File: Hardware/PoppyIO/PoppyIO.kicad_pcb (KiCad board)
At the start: 2 copper layers, 102 x 86 mm, 0 parts

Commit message: hw: io: Some PCB planning
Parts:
- added D10: Green, LED_SMD:LED_0805_2012Metric_Pad1.15x1.40mm_HandSolder, F.Cu at (132.4, 85.0)
- added D11: Green, LED_SMD:LED_0805_2012Metric_Pad1.15x1.40mm_HandSolder, F.Cu at (134.9, 85.0)
- added D12: Green, LED_SMD:LED_0805_2012Metric_Pad1.15x1.40mm_HandSolder, F.Cu at (137.5, 85.0)
- added D13: Green, LED_SMD:LED_0805_2012Metric_Pad1.15x1.40mm_HandSolder, F.Cu at (140.0, 85.0)
- added D14: Green, LED_SMD:LED_0805_2012Metric_Pad1.15x1.40mm_HandSolder, F.Cu at (145.4, 85.0)
- added D15: Green, LED_SMD:LED_0805_2012Metric_Pad1.15x1.40mm_HandSolder, F.Cu at (147.9, 85.0)
- added D16: Green, LED_SMD:LED_0805_2012Metric_Pad1.15x1.40mm_HandSolder, F.Cu at (150.5, 85.0)
- added D17: Green, LED_SMD:LED_0805_2012Metric_Pad1.15x1.40mm_HandSolder, F.Cu at (153.0, 85.0)
- added D18: Green, LED_SMD:LED_0805_2012Metric_Pad1.15x1.40mm_HandSolder, F.Cu at (106.4, 115.0)
- added D19: Green, LED_SMD:LED_0805_2012Metric_Pad1.15x1.40mm_HandSolder, F.Cu at (108.9, 115.0)
- added D2: Green, LED_SMD:LED_0805_2012Metric_Pad1.15x1.40mm_HandSolder, F.Cu at (106.4, 85.0)
- added D20: Green, LED_SMD:LED_0805_2012Metric_Pad1.15x1.40mm_HandSolder, F.Cu at (111.5, 115.0)
- added D21: Green, LED_SMD:LED_0805_2012Metric_Pad1.15x1.40mm_HandSolder, F.Cu at (114.0, 115.0)
- added D22: Green, LED_SMD:LED_0805_2012Metric_Pad1.15x1.40mm_HandSolder, F.Cu at (119.4, 115.0)
- added D23: Green, LED_SMD:LED_0805_2012Metric_Pad1.15x1.40mm_HandSolder, F.Cu at (121.9, 115.0)
- added D24: Green, LED_SMD:LED_0805_2012Metric_Pad1.15x1.40mm_HandSolder, F.Cu at (124.5, 115.0)
- added D25: Green, LED_SMD:LED_0805_2012Metric_Pad1.15x1.40mm_HandSolder, F.Cu at (127.0, 115.0)
- added D26: Green, LED_SMD:LED_0805_2012Metric_Pad1.15x1.40mm_HandSolder, F.Cu at (132.4, 115.0)
- added D27: Green, LED_SMD:LED_0805_2012Metric_Pad1.15x1.40mm_HandSolder, F.Cu at (134.9, 115.0)
- added D28: Green, LED_SMD:LED_0805_2012Metric_Pad1.15x1.40mm_HandSolder, F.Cu at (137.5, 115.0)
- added D29: Green, LED_SMD:LED_0805_2012Metric_Pad1.15x1.40mm_HandSolder, F.Cu at (140.0, 115.0)
- added D3: Green, LED_SMD:LED_0805_2012Metric_Pad1.15x1.40mm_HandSolder, F.Cu at (108.9, 85.0)
- added D30: Green, LED_SMD:LED_0805_2012Metric_Pad1.15x1.40mm_HandSolder, F.Cu at (145.4, 115.0)
- added D31: Green, LED_SMD:LED_0805_2012Metric_Pad1.15x1.40mm_HandSolder, F.Cu at (147.9, 115.0)
- added D32: Green, LED_SMD:LED_0805_2012Metric_Pad1.15x1.40mm_HandSolder, F.Cu at (150.5, 115.0)
- added D33: Green, LED_SMD:LED_0805_2012Metric_Pad1.15x1.40mm_HandSolder, F.Cu at (153.0, 115.0)
- added D4: Green, LED_SMD:LED_0805_2012Metric_Pad1.15x1.40mm_HandSolder, F.Cu at (111.5, 85.0)
- added D5: Green, LED_SMD:LED_0805_2012Metric_Pad1.15x1.40mm_HandSolder, F.Cu at (114.0, 85.0)
- added D6: Green, LED_SMD:LED_0805_2012Metric_Pad1.15x1.40mm_HandSolder, F.Cu at (119.4, 85.0)
- added D7: Green, LED_SMD:LED_0805_2012Metric_Pad1.15x1.40mm_HandSolder, F.Cu at (121.9, 85.0)
- added D8: Green, LED_SMD:LED_0805_2012Metric_Pad1.15x1.40mm_HandSolder, F.Cu at (124.5, 85.0)
- added D9: Green, LED_SMD:LED_0805_2012Metric_Pad1.15x1.40mm_HandSolder, F.Cu at (127.0, 85.0)
- added J1: TC2030-IDC, Connector:Tag-Connect_TC2030-IDC-FP_2x03_P1.27mm_Vertical, F.Cu at (169.0, 83.0)
- added J10: WAGO 233-508, PoppyLogicController:WAGO_233-204, F.Cu at (132.4, 135.0)
- added J11: WAGO 233-508, PoppyLogicController:WAGO_233-204, F.Cu at (145.4, 135.0)
- added J12: Conn_02x04_Counter_Clockwise, Connector_PinHeader_2.54mm:PinHeader_2x04_P2.54mm_Vertical, F.Cu at (194.7, 76.2)
- added J2: WAGO 233-508, PoppyLogicController:WAGO_233-204, F.Cu at (193.6, 65.0)
- added J3: WAGO 233-508, PoppyLogicController:WAGO_233-204, F.Cu at (114.0, 65.0)
- added J4: WAGO 233-508, PoppyLogicController:WAGO_233-204, F.Cu at (127.0, 65.0)
- added J5: WAGO 233-508, PoppyLogicController:WAGO_233-204, F.Cu at (140.0, 65.0)
- added J6: WAGO 233-508, PoppyLogicController:WAGO_233-204, F.Cu at (153.0, 65.0)
- added J7: WAGO 233-508, PoppyLogicController:WAGO_233-204, F.Cu at (186.0, 135.0)
- added J8: WAGO 233-508, PoppyLogicController:WAGO_233-204, F.Cu at (106.4, 135.0)
- added J9: WAGO 233-508, PoppyLogicController:WAGO_233-204, F.Cu at (119.4, 135.0)
- added R13: 1k, Resistor_SMD:R_0603_1608Metric_Pad0.98x0.95mm_HandSolder, F.Cu at (106.4, 80.0)
- added R14: 1k, Resistor_SMD:R_0603_1608Metric_Pad0.98x0.95mm_HandSolder, F.Cu at (108.9, 80.0)
- added R19: 1k, Resistor_SMD:R_0603_1608Metric_Pad0.98x0.95mm_HandSolder, F.Cu at (111.5, 80.0)
- added R20: 1k, Resistor_SMD:R_0603_1608Metric_Pad0.98x0.95mm_HandSolder, F.Cu at (114.0, 80.0)
- added R25: 1k, Resistor_SMD:R_0603_1608Metric_Pad0.98x0.95mm_HandSolder, F.Cu at (119.4, 80.0)
- added R26: 1k, Resistor_SMD:R_0603_1608Metric_Pad0.98x0.95mm_HandSolder, F.Cu at (121.9, 80.0)
- added R31: 1k, Resistor_SMD:R_0603_1608Metric_Pad0.98x0.95mm_HandSolder, F.Cu at (124.5, 80.0)
- added R32: 1k, Resistor_SMD:R_0603_1608Metric_Pad0.98x0.95mm_HandSolder, F.Cu at (127.0, 80.0)
- added R37: 1k, Resistor_SMD:R_0603_1608Metric_Pad0.98x0.95mm_HandSolder, F.Cu at (132.4, 80.0)
- added R38: 1k, Resistor_SMD:R_0603_1608Metric_Pad0.98x0.95mm_HandSolder, F.Cu at (134.9, 80.0)
- added R43: 1k, Resistor_SMD:R_0603_1608Metric_Pad0.98x0.95mm_HandSolder, F.Cu at (137.5, 80.0)
- added R44: 1k, Resistor_SMD:R_0603_1608Metric_Pad0.98x0.95mm_HandSolder, F.Cu at (140.0, 80.0)
- added R49: 1k, Resistor_SMD:R_0603_1608Metric_Pad0.98x0.95mm_HandSolder, F.Cu at (145.4, 80.0)
- added R50: 1k, Resistor_SMD:R_0603_1608Metric_Pad0.98x0.95mm_HandSolder, F.Cu at (147.9, 80.0)
- added R55: 1k, Resistor_SMD:R_0603_1608Metric_Pad0.98x0.95mm_HandSolder, F.Cu at (150.5, 80.0)
- added R56: 1k, Resistor_SMD:R_0603_1608Metric_Pad0.98x0.95mm_HandSolder, F.Cu at (153.0, 80.0)
- added R57: 1k, Resistor_SMD:R_0603_1608Metric_Pad0.98x0.95mm_HandSolder, F.Cu at (106.4, 120.0)
- added R58: 1k, Resistor_SMD:R_0603_1608Metric_Pad0.98x0.95mm_HandSolder, F.Cu at (108.9, 120.0)
- added R59: 1k, Resistor_SMD:R_0603_1608Metric_Pad0.98x0.95mm_HandSolder, F.Cu at (111.5, 120.0)
- added R60: 1k, Resistor_SMD:R_0603_1608Metric_Pad0.98x0.95mm_HandSolder, F.Cu at (114.0, 120.0)
- added R61: 1k, Resistor_SMD:R_0603_1608Metric_Pad0.98x0.95mm_HandSolder, F.Cu at (119.4, 120.0)
- added R62: 1k, Resistor_SMD:R_0603_1608Metric_Pad0.98x0.95mm_HandSolder, F.Cu at (121.9, 120.0)
- added R63: 1k, Resistor_SMD:R_0603_1608Metric_Pad0.98x0.95mm_HandSolder, F.Cu at (124.5, 120.0)
- added R64: 1k, Resistor_SMD:R_0603_1608Metric_Pad0.98x0.95mm_HandSolder, F.Cu at (127.0, 120.0)
- added R65: 1k, Resistor_SMD:R_0603_1608Metric_Pad0.98x0.95mm_HandSolder, F.Cu at (132.4, 120.0)
- added R66: 1k, Resistor_SMD:R_0603_1608Metric_Pad0.98x0.95mm_HandSolder, F.Cu at (134.9, 120.0)
- added R67: 1k, Resistor_SMD:R_0603_1608Metric_Pad0.98x0.95mm_HandSolder, F.Cu at (137.5, 120.0)
- added R68: 1k, Resistor_SMD:R_0603_1608Metric_Pad0.98x0.95mm_HandSolder, F.Cu at (140.0, 120.0)
- added R69: 1k, Resistor_SMD:R_0603_1608Metric_Pad0.98x0.95mm_HandSolder, F.Cu at (145.4, 120.0)
- added R70: 1k, Resistor_SMD:R_0603_1608Metric_Pad0.98x0.95mm_HandSolder, F.Cu at (147.9, 120.0)
- added R71: 1k, Resistor_SMD:R_0603_1608Metric_Pad0.98x0.95mm_HandSolder, F.Cu at (150.5, 120.0)
- added R72: 1k, Resistor_SMD:R_0603_1608Metric_Pad0.98x0.95mm_HandSolder, F.Cu at (153.0, 120.0)
- added SW1: PTS645SH43SMTR92LFS, Button_Switch_SMD:SW_SPST_PTS645, F.Cu at (188.0, 100.0)
- added U1: Pico, RPi_Pico:RPi_Pico_SMD_TH, F.Cu at (169.0, 117.0)
- added U2: PCA9555PW, Package_SO:TSSOP-24_4.4x7.8mm_P0.65mm, F.Cu at (129.0, 95.0)
- added U3: PCA9555PW, Package_SO:TSSOP-24_4.4x7.8mm_P0.65mm, F.Cu at (129.0, 105.0)
- added U4: ULQ2003A, Package_SO:SOIC-16_3.9x9.9mm_P1.27mm, F.Cu at (113.0, 128.0)
- added U5: ULQ2003A, Package_SO:SOIC-16_3.9x9.9mm_P1.27mm, F.Cu at (126.0, 128.0)
- added U6: ULQ2003A, Package_SO:SOIC-16_3.9x9.9mm_P1.27mm, F.Cu at (139.0, 128.0)

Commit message: hw: ui: Adjust connector pin ordering
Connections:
- J3 pad 1: I00_HIGH -> I03_HIGH
- J3 pad 2: I01_HIGH -> I02_HIGH
- J3 pad 3: I02_HIGH -> I01_HIGH
- J3 pad 4: I03_HIGH -> I00_HIGH
- J4 pad 1: I04_HIGH -> I07_HIGH
- J4 pad 2: I05_HIGH -> I06_HIGH
- J4 pad 3: I06_HIGH -> I05_HIGH
- J4 pad 4: I07_HIGH -> I04_HIGH
- J5 pad 1: I08_HIGH -> I11_HIGH
- J5 pad 2: I09_HIGH -> I10_HIGH
- J5 pad 3: I10_HIGH -> I09_HIGH
- J5 pad 4: I11_HIGH -> I08_HIGH
- J6 pad 1: I12_HIGH -> I15_HIGH
- J6 pad 2: I13_HIGH -> I14_HIGH
- J6 pad 3: I14_HIGH -> I13_HIGH
- J6 pad 4: I15_HIGH -> I12_HIGH
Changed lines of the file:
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@@
     (fp_rect (start -2.54 -2.6) (end 9.07 7.7) (layer "F.Fab") (width 0.1) (fill none))
     (pad "1" thru_hole roundrect locked (at 0 5 180) (size 2 2) (drill 1.1) (layers *.Cu *.Mask) (roundrect_rratio 0.25)
-      (net 62 "I04_HIGH") (pinfunction "Pin_1") (pintype "passive"))
+      (net 65 "I07_HIGH") (pinfunction "Pin_1") (pintype "passive"))
     (pad "1" thru_hole roundrect locked (at 0 0 180) (size 2 2) (drill 1.1) (layers *.Cu *.Mask) (roundrect_rratio 0.25)
-      (net 62 "I04_HIGH") (pinfunction "Pin_1") (pintype "passive"))
+      (net 65 "I07_HIGH") (pinfunction "Pin_1") (pintype "passive"))
     (pad "2" thru_hole circle locked (at 2.54 5 180) (size 2 2) (drill 1.1) (layers *.Cu *.Mask)
-      (net 63 "I05_HIGH") (pinfunction "Pin_2") (pintype "passive"))
+      (net 64 "I06_HIGH") (pinfunction "Pin_2") (pintype "passive"))
     (pad "2" thru_hole circle locked (at 2.54 0 180) (size 2 2) (drill 1.1) (layers *.Cu *.Mask)
-      (net 63 "I05_HIGH") (pinfunction "Pin_2") (pintype "passive"))
+      (net 64 "I06_HIGH") (pinfunction "Pin_2") (pintype "passive"))
     (pad "3" thru_hole circle locked (at 5.08 5 180) (size 2 2) (drill 1.1) (layers *.Cu *.Mask)
-      (net 64 "I06_HIGH") (pinfunction "Pin_3") (pintype "passive"))
+      (net 63 "I05_HIGH") (pinfunction "Pin_3") (pintype "passive"))
     (pad "3" thru_hole circle locked (at 5.08 0 180) (size 2 2) (drill 1.1) (layers *.Cu *.Mask)
-      (net 64 "I06_HIGH") (pinfunction "Pin_3") (pintype "passive"))
+      (net 63 "I05_HIGH") (pinfunction "Pin_3") (pintype "passive"))
     (pad "4" thru_hole circle locked (at 7.62 5 180) (size 2 2) (drill 1.1) (layers *.Cu *.Mask)
-      (net 65 "I07_HIGH") (pinfunction "Pin_4") (pintype "passive"))
+      (net 62 "I04_HIGH") (pinfunction "Pin_4") (pintype "passive"))
     (pad "4" thru_hole circle locked (at 7.62 0 180) (size 2 2) (drill 1.1) (layers *.Cu *.Mask)
-      (net 65 "I07_HIGH") (pinfunction "Pin_4") (pintype "passive"))
+      (net 62 "I04_HIGH") (pinfunction "Pin_4") (pintype "passive"))
     (model "${KIPRJMOD}/../Libraries/3D/233-504.step"
       (offset (xyz 9 -5 0))
@@
     (fp_rect (start -2.54 -2.6) (end 9.07 7.7) (layer "F.Fab") (width 0.1) (fill none))
     (pad "1" thru_hole roundrect locked (at 0 0 180) (size 2 2) (drill 1.1) (layers *.Cu *.Mask) (roundrect_rratio 0.25)
-      (net 66 "I08_HIGH") (pinfunction "Pin_1") (pintype "passive"))
+      (net 69 "I11_HIGH") (pinfunction "Pin_1") (pintype "passive"))
     (pad "1" thru_hole roundrect locked (at 0 5 180) (size 2 2) (drill 1.1) (layers *.Cu *.Mask) (roundrect_rratio 0.25)
-      (net 66 "I08_HIGH") (pinfunction "Pin_1") (pintype "passive"))
+      (net 69 "I11_HIGH") (pinfunction "Pin_1") (pintype "passive"))
     (pad "2" thru_hole circle locked (at 2.54 5 180) (size 2 2) (drill 1.1) (layers *.Cu *.Mask)
-      (net 67 "I09_HIGH") (pinfunction "Pin_2") (pintype "passive"))
+      (net 68 "I10_HIGH") (pinfunction "Pin_2") (pintype "passive"))
     (pad "2" thru_hole circle locked (at 2.54 0 180) (size 2 2) (drill 1.1) (layers *.Cu *.Mask)
-      (net 67 "I09_HIGH") (pinfunction "Pin_2") (pintype "passive"))
+      (net 68 "I10_HIGH") (pinfunction "Pin_2") (pintype "passive"))
     (pad "3" thru_hole circle locked (at 5.08 0 180) (size 2 2) (drill 1.1) (layers *.Cu *.Mask)
-      (net 68 "I10_HIGH") (pinfunction "Pin_3") (pintype "passive"))
+      (net 67 "I09_HIGH") (pinfunction "Pin_3") (pintype "passive"))
     (pad "3" thru_hole circle locked (at 5.08 5 180) (size 2 2) (drill 1.1) (layers *.Cu *.Mask)
-      (net 68 "I10_HIGH") (pinfunction "Pin_3") (pintype "passive"))
+      (net 67 "I09_HIGH") (pinfunction "Pin_3") (pintype "passive"))
     (pad "4" thru_hole circle locked (at 7.62 5 180) (size 2 2) (drill 1.1) (layers *.Cu *.Mask)
-      (net 69 "I11_HIGH") (pinfunction "Pin_4") (pintype "passive"))
+      (net 66 "I08_HIGH") (pinfunction "Pin_4") (pintype "passive"))
     (pad "4" thru_hole circle locked (at 7.62 0 180) (size 2 2) (drill 1.1) (layers *.Cu *.Mask)
-      (net 69 "I11_HIGH") (pinfunction "Pin_4") (pintype "passive"))
+      (net 66 "I08_HIGH") (pinfunction "Pin_4") (pintype "passive"))
     (model "${KIPRJMOD}/../Libraries/3D/233-504.step"
       (offset (xyz 9 -5 0))
@@
     (fp_rect (start -2.54 -2.6) (end 9.07 7.7) (layer "F.Fab") (width 0.1) (fill none))
     (pad "1" thru_hole roundrect locked (at 0 5 180) (size 2 2) (drill 1.1) (layers *.Cu *.Mask) (roundrect_rratio 0.25)
-      (net 58 "I00_HIGH") (pinfunction "Pin_1") (pintype "passive"))
+      (net 61 "I03_HIGH") (pinfunction "Pin_1") (pintype "passive"))
     (pad "1" thru_hole roundrect locked (at 0 0 180) (size 2 2) (drill 1.1) (layers *.Cu *.Mask) (roundrect_rratio 0.25)
-      (net 58 "I00_HIGH") (pinfunction "Pin_1") (pintype "passive"))
+      (net 61 "I03_HIGH") (pinfunction "Pin_1") (pintype "passive"))
     (pad "2" thru_hole circle locked (at 2.54 0 180) (size 2 2) (drill 1.1) (layers *.Cu *.Mask)
-      (net 59 "I01_HIGH") (pinfunction "Pin_2") (pintype "passive"))
+      (net 60 "I02_HIGH") (pinfunction "Pin_2") (pintype "passive"))
     (pad "2" thru_hole circle locked (at 2.54 5 180) (size 2 2) (drill 1.1) (layers *.Cu *.Mask)
-      (net 59 "I01_HIGH") (pinfunction "Pin_2") (pintype "passive"))
+      (net 60 "I02_HIGH") (pinfunction "Pin_2") (pintype "passive"))
     (pad "3" thru_hole circle locked (at 5.08 5 180) (size 2 2) (drill 1.1) (layers *.Cu *.Mask)
-      (net 60 "I02_HIGH") (pinfunction "Pin_3") (pintype "passive"))
+      (net 59 "I01_HIGH") (pinfunction "Pin_3") (pintype "passive"))
     (pad "3" thru_hole circle locked (at 5.08 0 180) (size 2 2) (drill 1.1) (layers *.Cu *.Mask)
-      (net 60 "I02_HIGH") (pinfunction "Pin_3") (pintype "passive"))
+      (net 59 "I01_HIGH") (pinfunction "Pin_3") (pintype "passive"))
     (pad "4" thru_hole circle locked (at 7.62 0 180) (size 2 2) (drill 1.1) (layers *.Cu *.Mask)
-      (net 61 "I03_HIGH") (pinfunction "Pin_4") (pintype "passive"))
+      (net 58 "I00_HIGH") (pinfunction "Pin_4") (pintype "passive"))
     (pad "4" thru_hole circle locked (at 7.62 5 180) (size 2 2) (drill 1.1) (layers *.Cu *.Mask)
-      (net 61 "I03_HIGH") (pinfunction "Pin_4") (pintype "passive"))
+      (net 58 "I00_HIGH") (pinfunction "Pin_4") (pintype "passive"))
     (model "${KIPRJMOD}/../Libraries/3D/233-504.step"
       (offset (xyz 9 -5 0))
@@
     (fp_rect (start -2.54 -2.6) (end 9.07 7.7) (layer "F.Fab") (width 0.1) (fill none))
     (pad "1" thru_hole roundrect locked (at 0 5 180) (size 2 2) (drill 1.1) (layers *.Cu *.Mask) (roundrect_rratio 0.25)
-      (net 70 "I12_HIGH") (pinfunction "Pin_1") (pintype "passive"))
+      (net 73 "I15_HIGH") (pinfunction "Pin_1") (pintype "passive"))
     (pad "1" thru_hole roundrect locked (at 0 0 180) (size 2 2) (drill 1.1) (layers *.Cu *.Mask) (roundrect_rratio 0.25)
-      (net 70 "I12_HIGH") (pinfunction "Pin_1") (pintype "passive"))
+      (net 73 "I15_HIGH") (pinfunction "Pin_1") (pintype "passive"))
     (pad "2" thru_hole circle locked (at 2.54 5 180) (size 2 2) (drill 1.1) (layers *.Cu *.Mask)
-      (net 71 "I13_HIGH") (pinfunction "Pin_2") (pintype "passive"))
+      (net 72 "I14_HIGH") (pinfunction "Pin_2") (pintype "passive"))
     (pad "2" thru_hole circle locked (at 2.54 0 180) (size 2 2) (drill 1.1) (layers *.Cu *.Mask)
-      (net 71 "I13_HIGH") (pinfunction "Pin_2") (pintype "passive"))
+      (net 72 "I14_HIGH") (pinfunction "Pin_2") (pintype "passive"))
     (pad "3" thru_hole circle locked (at 5.08 0 180) (size 2 2) (drill 1.1) (layers *.Cu *.Mask)
-      (net 72 "I14_HIGH") (pinfunction "Pin_3") (pintype "passive"))
+      (net 71 "I13_HIGH") (pinfunction "Pin_3") (pintype "passive"))
     (pad "3" thru_hole circle locked (at 5.08 5 180) (size 2 2) (drill 1.1) (layers *.Cu *.Mask)
-      (net 72 "I14_HIGH") (pinfunction "Pin_3") (pintype "passive"))
+      (net 71 "I13_HIGH") (pinfunction "Pin_3") (pintype "passive"))
     (pad "4" thru_hole circle locked (at 7.62 0 180) (size 2 2) (drill 1.1) (layers *.Cu *.Mask)
-      (net 73 "I15_HIGH") (pinfunction "Pin_4") (pintype "passive"))
+      (net 70 "I12_HIGH") (pinfunction "Pin_4") (pintype "passive"))
     (pad "4" thru_hole circle locked (at 7.62 5 180) (size 2 2) (drill 1.1) (layers *.Cu *.Mask)
-      (net 73 "I15_HIGH") (pinfunction "Pin_4") (pintype "passive"))
+      (net 70 "I12_HIGH") (pinfunction "Pin_4") (pintype "passive"))
     (model "${KIPRJMOD}/../Libraries/3D/233-504.step"
       (offset (xyz 9 -5 0))

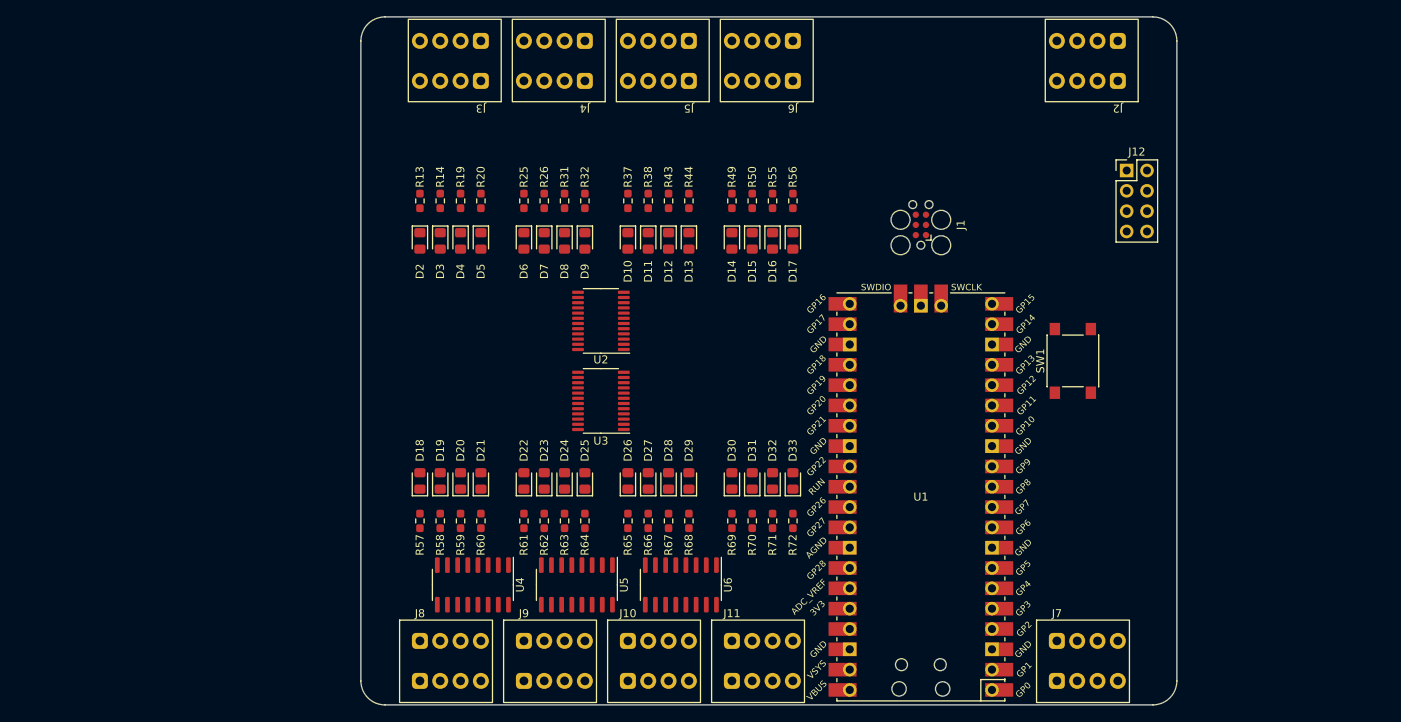
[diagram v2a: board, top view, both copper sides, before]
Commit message: hw: io: More layout improvements
Reorder driver pins
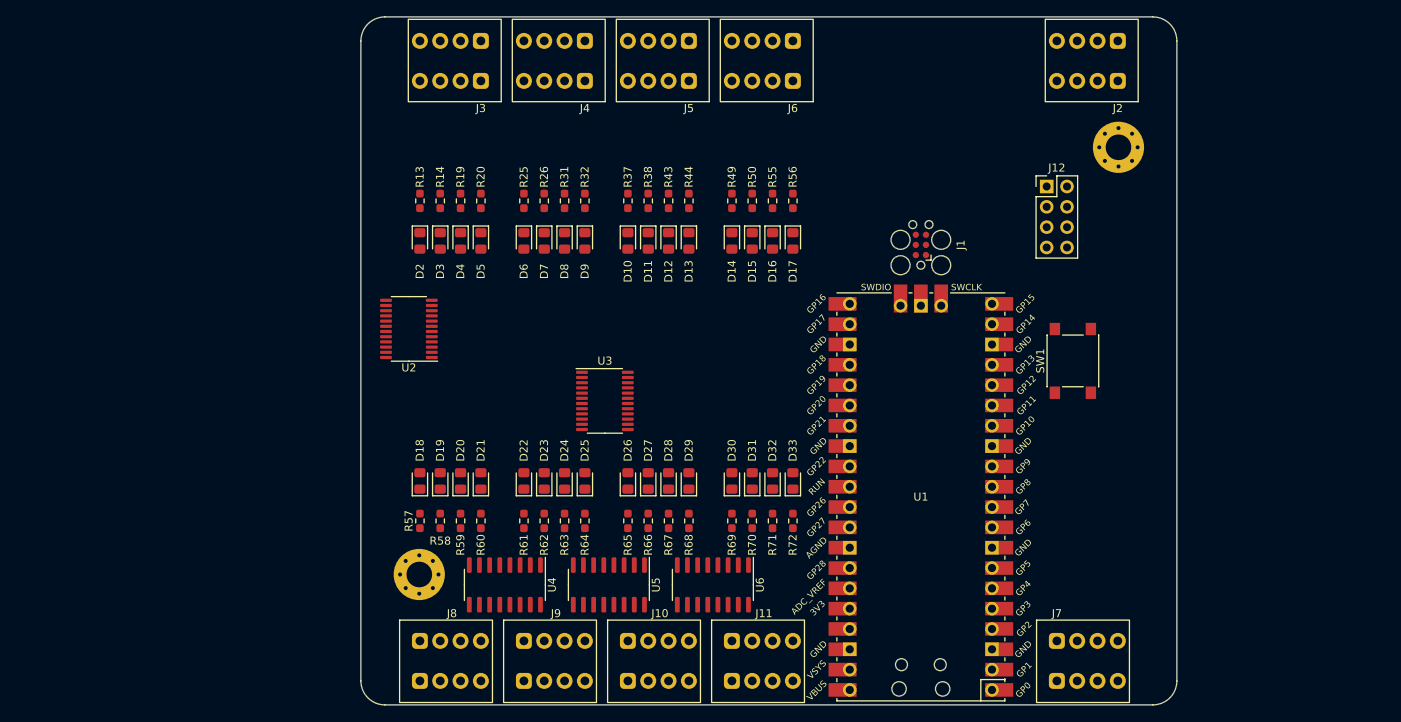
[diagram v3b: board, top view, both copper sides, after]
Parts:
- added H1: MountingHole_Pad, MountingHole:MountingHole_3.2mm_M3_Pad_Via, F.Cu at (193.7, 73.3)
- added H2: MountingHole_Pad, MountingHole:MountingHole_3.2mm_M3_Pad_Via, F.Cu at (106.3, 126.7)
- moved U2 24.0 mm to (105.0, 96.0)
- moved J12 10.2 mm to (184.7, 78.2)
- moved U4 4.00 mm to (117.0, 128.0)
- moved U5 4.00 mm to (130.0, 128.0)
- moved U6 4.00 mm to (143.0, 128.0)
- moved J1 2.50 mm to (169.0, 85.5)
- moved U3 0.50 mm to (129.5, 105.0), turned to 0 degrees
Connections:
- U4 pad 1: /O00_LOW -> /O06_LOW
- U4 pad 10: O06_HIGH -> O00_HIGH
- U4 pad 11: O05_HIGH -> O01_HIGH
- U4 pad 12: O04_HIGH -> O02_HIGH
- U4 pad 14: O02_HIGH -> O04_HIGH
- U4 pad 15: O01_HIGH -> O05_HIGH
- U4 pad 16: O00_HIGH -> O06_HIGH
- U4 pad 2: /O01_LOW -> /O05_LOW
- U4 pad 3: /O02_LOW -> /O04_LOW
- U4 pad 5: /O04_LOW -> /O02_LOW
- U4 pad 6: /O05_LOW -> /O01_LOW
- U4 pad 7: /O06_LOW -> /O00_LOW
- U5 pad 1: /O07_LOW -> /O13_LOW
- U5 pad 10: O13_HIGH -> O07_HIGH
- U5 pad 11: O12_HIGH -> O08_HIGH
- U5 pad 12: O11_HIGH -> O09_HIGH
- U5 pad 14: O09_HIGH -> O11_HIGH
- U5 pad 15: O08_HIGH -> O12_HIGH
- U5 pad 16: O07_HIGH -> O13_HIGH
- U5 pad 2: /O08_LOW -> /O12_LOW
- U5 pad 3: /O09_LOW -> /O11_LOW
- U5 pad 5: /O11_LOW -> /O09_LOW
- U5 pad 6: /O12_LOW -> /O08_LOW
- U5 pad 7: /O13_LOW -> /O07_LOW
- U6 pad 1: /O14_LOW -> /O15_LOW
- U6 pad 15: O15_HIGH -> O14_HIGH
- U6 pad 16: O14_HIGH -> O15_HIGH
- U6 pad 2: /O15_LOW -> /O14_LOW

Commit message: hw: io: Updates
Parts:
- added Q1: FC6946010R, Package_TO_SOT_SMD:SOT-666, F.Cu at (107.7, 76.7)
- added Q2: FC6946010R, Package_TO_SOT_SMD:SOT-666, F.Cu at (112.7, 76.7)
- added Q3: FC6946010R, Package_TO_SOT_SMD:SOT-666, F.Cu at (120.5, 73.5)
- added Q4: FC6946010R, Package_TO_SOT_SMD:SOT-666, F.Cu at (126.5, 73.5)
- added Q5: FC6946010R, Package_TO_SOT_SMD:SOT-666, F.Cu at (134.0, 73.5)
- added Q6: FC6946010R, Package_TO_SOT_SMD:SOT-666, F.Cu at (140.0, 73.5)
- added Q7: FC6946010R, Package_TO_SOT_SMD:SOT-666, F.Cu at (146.5, 73.5)
- added Q8: FC6946010R, Package_TO_SOT_SMD:SOT-666, F.Cu at (151.5, 73.5)
- added R10: 100k, Resistor_SMD:R_0603_1608Metric_Pad0.98x0.95mm_HandSolder, F.Cu at (106.4, 73.6)
- added R11: 680k, Resistor_SMD:R_0603_1608Metric_Pad0.98x0.95mm_HandSolder, F.Cu at (108.9, 70.1)
- added R12: 100k, Resistor_SMD:R_0603_1608Metric_Pad0.98x0.95mm_HandSolder, F.Cu at (108.9, 73.6)
- added R15: 680k, Resistor_SMD:R_0603_1608Metric_Pad0.98x0.95mm_HandSolder, F.Cu at (111.5, 70.1)
- added R16: 100k, Resistor_SMD:R_0603_1608Metric_Pad0.98x0.95mm_HandSolder, F.Cu at (111.5, 73.6)
- added R17: 680k, Resistor_SMD:R_0603_1608Metric_Pad0.98x0.95mm_HandSolder, F.Cu at (114.0, 70.1)
- added R18: 100k, Resistor_SMD:R_0603_1608Metric_Pad0.98x0.95mm_HandSolder, F.Cu at (114.0, 73.6)
- added R9: 680k, Resistor_SMD:R_0603_1608Metric_Pad0.98x0.95mm_HandSolder, F.Cu at (106.4, 70.1)
- moved U2 24.6 mm to (129.5, 94.0), turned to 0 degrees
- turned R14 to 90 degrees
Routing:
- net /I02_LOW: track 0.00 -> 21.7 mm, vias 0 -> 2
- net /I00_LOW: track 0.00 -> 21.7 mm, vias 0 -> 2
- net /I03_LOW: track 0.00 -> 18.1 mm
- net /I01_LOW: track 0.00 -> 18.1 mm
- net GND: track 0.00 -> 14.9 mm, vias 0 -> 4
- net Net-(Q1-Pad3): track 0.00 -> 7.88 mm
- net Net-(Q2-Pad3): track 0.00 -> 7.78 mm
- net Net-(Q2-Pad6): track 0.00 -> 4.45 mm
- net Net-(Q1-Pad6): track 0.00 -> 4.45 mm
- net Net-(D5-Pad1): track 0.00 -> 3.06 mm
- net Net-(D4-Pad1): track 0.00 -> 3.06 mm
- net Net-(D3-Pad1): track 0.00 -> 3.06 mm
- net Net-(D2-Pad1): track 0.00 -> 3.06 mm
